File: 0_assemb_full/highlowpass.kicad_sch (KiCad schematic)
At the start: 19 parts, among them U3 LM2902, U4 LM2902

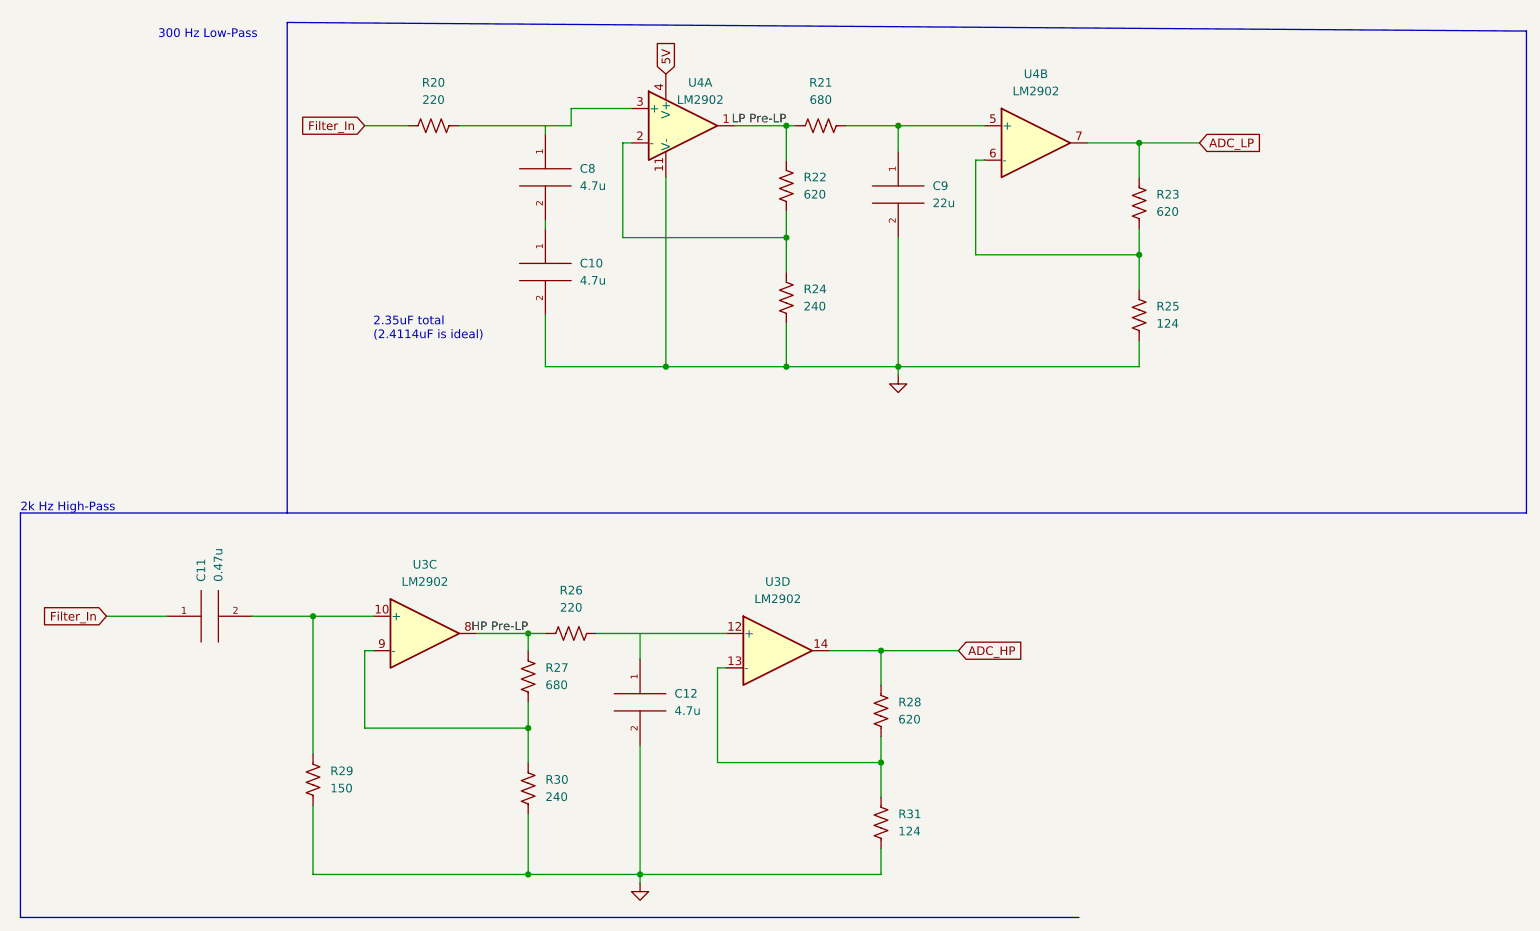
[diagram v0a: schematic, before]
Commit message: A lot of work done on the STM32 PCB layout.
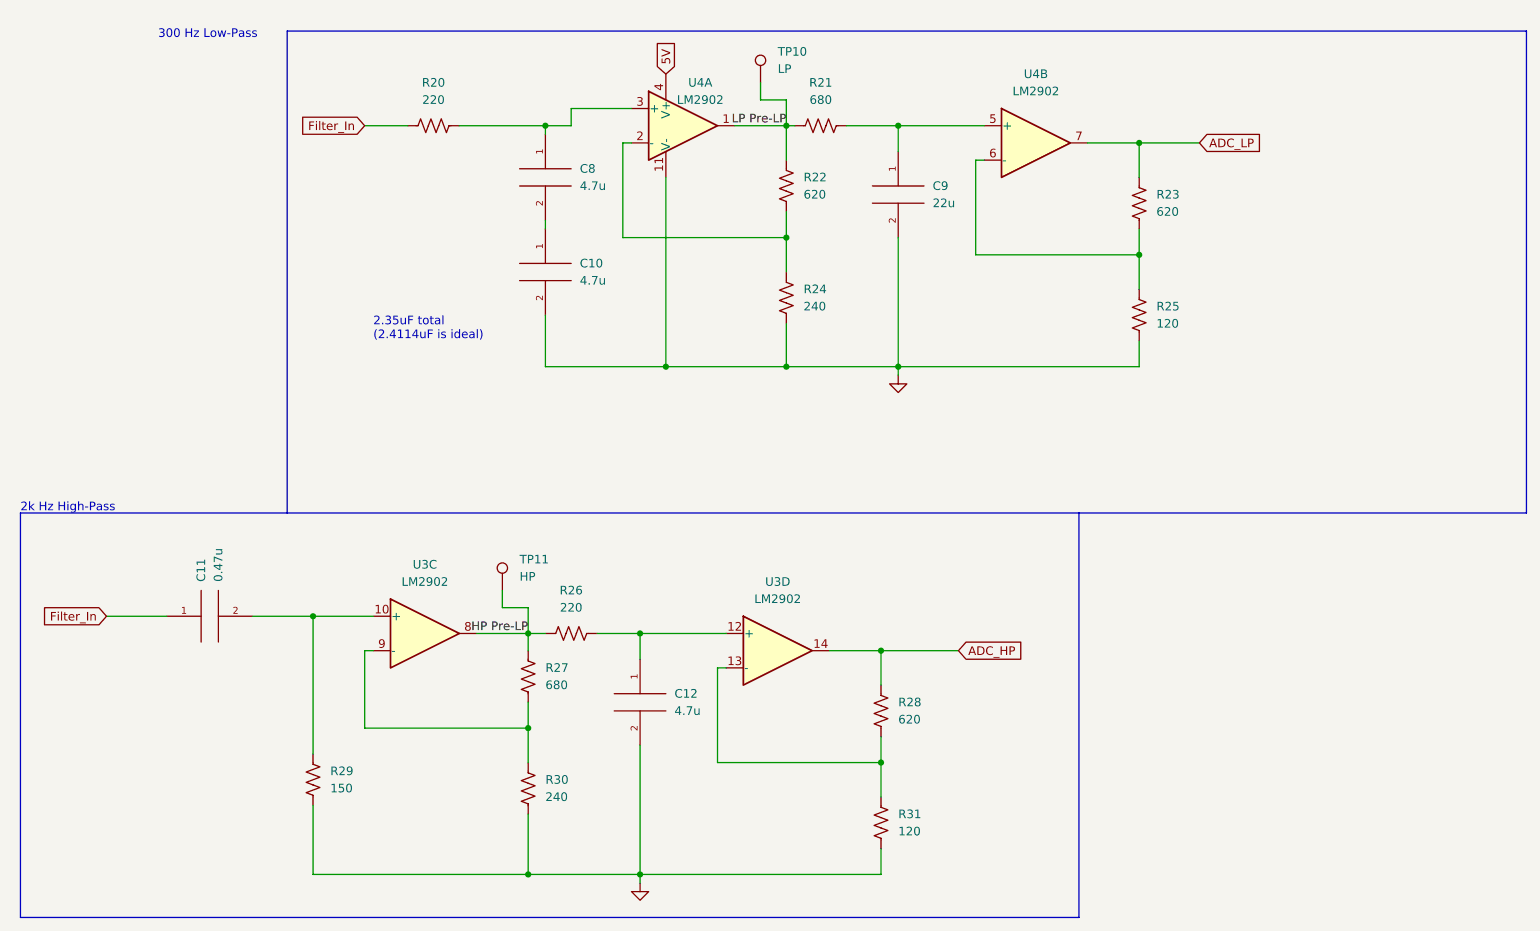
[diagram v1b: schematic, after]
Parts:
- added TP10: LP, TestPoint:TestPoint_THTPad_1.5x1.5mm_Drill0.7mm, symbol Connector:TestPoint
- added TP11: HP, TestPoint:TestPoint_THTPad_1.5x1.5mm_Drill0.7mm, symbol Connector:TestPoint
- C10, C12, C8: footprint (none) -> Capacitor_THT:C_Rect_L26.5mm_W7.0mm_P22.50mm_MKS4
- C11: footprint (none) -> Capacitor_THT:C_Rect_L7.2mm_W3.5mm_P5.00mm_FKS2_FKP2_MKS2_MKP2
- C9: footprint (none) -> Capacitor_SMD:CP_Elec_5x5.8
- R20, R21, R22, R23, R24, R26, R27, R28, R29, R30: footprint (none) -> Resistor_SMD:R_0805_2012Metric_Pad1.20x1.40mm_HandSolder
- R25, R31: value 124 -> 120; footprint (none) -> Resistor_SMD:R_0805_2012Metric_Pad1.20x1.40mm_HandSolder
- U3, U4: footprint (none) -> Package_DIP:DIP-14_W7.62mm
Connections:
- net HP Pre-LP: now also TP11.1
- net LP Pre-LP: now also TP10.1
- net at R26.2, U3.12 (+): now also C12.1
- net at R20.2, U4.3 (+): now also C8.1

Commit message: Some filter adjustments
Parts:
- added C53: 100n, Capacitor_SMD:C_0805_2012Metric_Pad1.18x1.45mm_HandSolder, symbol Device:C_Small
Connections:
- net 5V: now also C53.1
- net GND: now also C53.2
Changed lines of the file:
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@@
   (junction (at 179.07 31.75) (diameter 0) (color 0 0 0 0)
   )
+  (junction (at 109.22 17.78) (diameter 0) (color 0 0 0 0)
+  )
   (wire (pts (xy 143.51 45.72) (xy 143.51 64.77))
     (stroke (width 0) (type default) (color 0 0 0 0))
@@
     (stroke (width 0) (type default) (color 0 0 0 0))
   )
-  (polyline (pts (xy 236.22 86.36) (xy 236.22 15.24))
+  (polyline (pts (xy 236.22 86.36) (xy 236.22 12.7))
     (stroke (width 0) (type default) (color 0 0 0 0))
   )
@@
     (stroke (width 0) (type default) (color 0 0 0 0))
   )
-  (polyline (pts (xy 236.22 15.24) (xy 53.34 15.24))
+  (polyline (pts (xy 236.22 12.7) (xy 53.34 12.7))
     (stroke (width 0) (type default) (color 0 0 0 0))
   )
@@
     (stroke (width 0) (type default) (color 0 0 0 0))
   )
+  (wire (pts (xy 109.22 17.78) (xy 110.49 17.78))
+    (stroke (width 0) (type default) (color 0 0 0 0))
+  )
   (wire (pts (xy 127 29.21) (xy 127 34.29))
     (stroke (width 0) (type default) (color 0 0 0 0))
@@
     (stroke (width 0) (type default) (color 0 0 0 0))
   )
+  (wire (pts (xy 116.84 19.05) (xy 116.84 17.78))
+    (stroke (width 0) (type default) (color 0 0 0 0))
+  )
   (wire (pts (xy 88.9 100.33) (xy 88.9 104.14))
     (stroke (width 0) (type default) (color 0 0 0 0))
   )
-  (polyline (pts (xy 53.34 15.24) (xy 53.34 86.36))
+  (polyline (pts (xy 53.34 12.7) (xy 53.34 86.36))
     (stroke (width 0) (type default) (color 0 0 0 0))
   )
@@
     (stroke (width 0) (type default) (color 0 0 0 0))
   )
+  (wire (pts (xy 104.14 17.78) (xy 109.22 17.78))
+    (stroke (width 0) (type default) (color 0 0 0 0))
+  )
   (wire (pts (xy 104.14 31.75) (xy 102.87 31.75))
     (stroke (width 0) (type default) (color 0 0 0 0))
   )
+  (wire (pts (xy 116.84 17.78) (xy 115.57 17.78))
+    (stroke (width 0) (type default) (color 0 0 0 0))
+  )
   (wire (pts (xy 88.9 114.3) (xy 88.9 118.11))
     (stroke (width 0) (type default) (color 0 0 0 0))
@@
   )
   (wire (pts (xy 88.9 118.11) (xy 88.9 123.19))
+    (stroke (width 0) (type default) (color 0 0 0 0))
+  )
+  (wire (pts (xy 109.22 17.78) (xy 109.22 21.59))
     (stroke (width 0) (type default) (color 0 0 0 0))
   )
@@
     (effects (font (size 1.27 1.27)) (justify right bottom))
   )
-  (global_label "5V" (shape input) (at 109.22 21.59 90) (fields_autoplaced)
-    (effects (font (size 1.27 1.27)) (justify left))
-    (property "Intersheet References" "${INTERSHEET_REFS}" (id 0) (at 109.1406 16.8788 90)
-      (effects (font (size 1.27 1.27)) (justify left) hide)
+  (global_label "5V" (shape input) (at 104.14 17.78 180) (fields_autoplaced)
+    (effects (font (size 1.27 1.27)) (justify right))
+    (property "Intersheet References" "${INTERSHEET_REFS}" (id 0) (at 99.4288 17.8594 0)
+      (effects (font (size 1.27 1.27)) (justify right) hide)
     )
   )
@@
     (pin "2")
   )
+  (symbol (lib_id "Device:C_Small") (at 113.03 17.78 90) (unit 1)
+    (in_bom yes) (on_board yes)
+    (property "Reference" "C53" (id 0) (at 109.22 13.97 90))
+    (property "Value" "100n" (id 1) (at 109.22 16.51 90))
+    (property "Footprint" "Capacitor_SMD:C_0805_2012Metric_Pad1.18x1.45mm_HandSolder" (id 2) (at 113.03 17.78 0)
+      (effects (font (size 1.27 1.27)) hide)
+    )
+    (property "Datasheet" "~" (id 3) (at 113.03 17.78 0)
+      (effects (font (size 1.27 1.27)) hide)
+    )
+    (pin "1")
+    (pin "2")
+  )
   (symbol (lib_id "Amplifier_Operational:LM2902") (at 163.83 31.75 0) (unit 2)
     (in_bom yes) (on_board yes) (fields_autoplaced)
@@
     (pin "4")
   )
+  (symbol (lib_id "power:GND") (at 116.84 19.05 0) (unit 1)
+    (in_bom yes) (on_board yes) (fields_autoplaced)
+    (property "Reference" "#PWR048" (id 0) (at 116.84 25.4 0)
+      (effects (font (size 1.27 1.27)) hide)
+    )
+    (property "Value" "GND" (id 1) (at 116.84 24.13 0)
+      (effects (font (size 1.27 1.27)) hide)
+    )
+    (property "Footprint" "" (id 2) (at 116.84 19.05 0)
+      (effects (font (size 1.27 1.27)) hide)
+    )
+    (property "Datasheet" "" (id 3) (at 116.84 19.05 0)
+      (effects (font (size 1.27 1.27)) hide)
+    )
+    (pin "1")
+  )
   (symbol (lib_id "pspice:C") (at 105.41 114.3 0) (unit 1)

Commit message: Active Filters layout added
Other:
- title: High and Low Pass Filters with Bar Graph LEDs -> High and Low Pass Filter
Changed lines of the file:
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@@
   (paper "A4")
   (title_block
-    (title "High and Low Pass Filters with Bar Graph LEDs")
+    (title "High and Low Pass Filter")
   )
   (junction (at 88.9 139.7) (diameter 0) (color 0 0 0 0)

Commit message: Made adjustments according to presentation feedback. Almost ready for teaching team to look over.
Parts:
- TP10, TP11: footprint TestPoint:TestPoint_THTPad_1.5x1.5mm_Drill0.7mm -> TestPoint:TestPoint_THTPad_2.0x2.0mm_Drill1.0mm
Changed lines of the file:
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@@
       (effects (font (size 1.27 1.27)) (justify left))
     )
-    (property "Footprint" "TestPoint:TestPoint_THTPad_1.5x1.5mm_Drill0.7mm" (id 2) (at 128.27 22.86 0)
+    (property "Footprint" "TestPoint:TestPoint_THTPad_2.0x2.0mm_Drill1.0mm" (id 2) (at 128.27 22.86 0)
       (effects (font (size 1.27 1.27)) hide)
     )
@@
       (effects (font (size 1.27 1.27)) (justify left))
     )
-    (property "Footprint" "TestPoint:TestPoint_THTPad_1.5x1.5mm_Drill0.7mm" (id 2) (at 90.17 97.79 0)
-      (effects (font (size 1.27 1.27)) hide)
-    )
+    (property "Footprint" "TestPoint:TestPoint_THTPad_2.0x2.0mm_Drill1.0mm" (id 2) (at 90.17 97.79 0)
+      (effects (font (size 1.27 1.27)) hide)
+    )
